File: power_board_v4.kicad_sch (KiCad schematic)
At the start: 21 parts, among them J1 Conn_01x02, J2 Conn_01x02, J3 Conn_01x02, J4 Conn_01x02, J5 Conn_01x02, J6 Conn_01x02, J7 Conn_01x02, Q1 PMOS, Q2 2SC1815, Q3 PMOS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

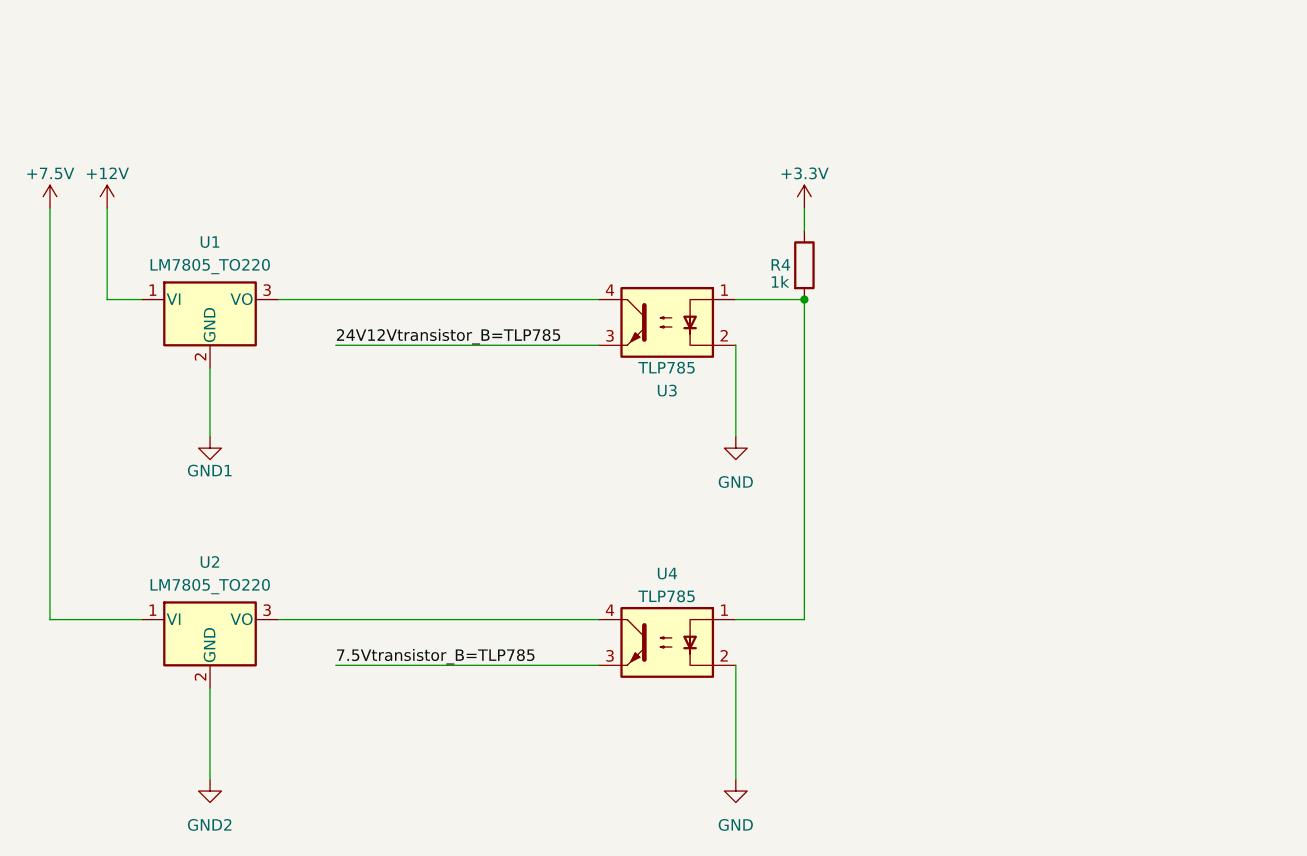
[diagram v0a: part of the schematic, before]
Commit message: レギュレーターとフォトカプラの周辺部品の追加
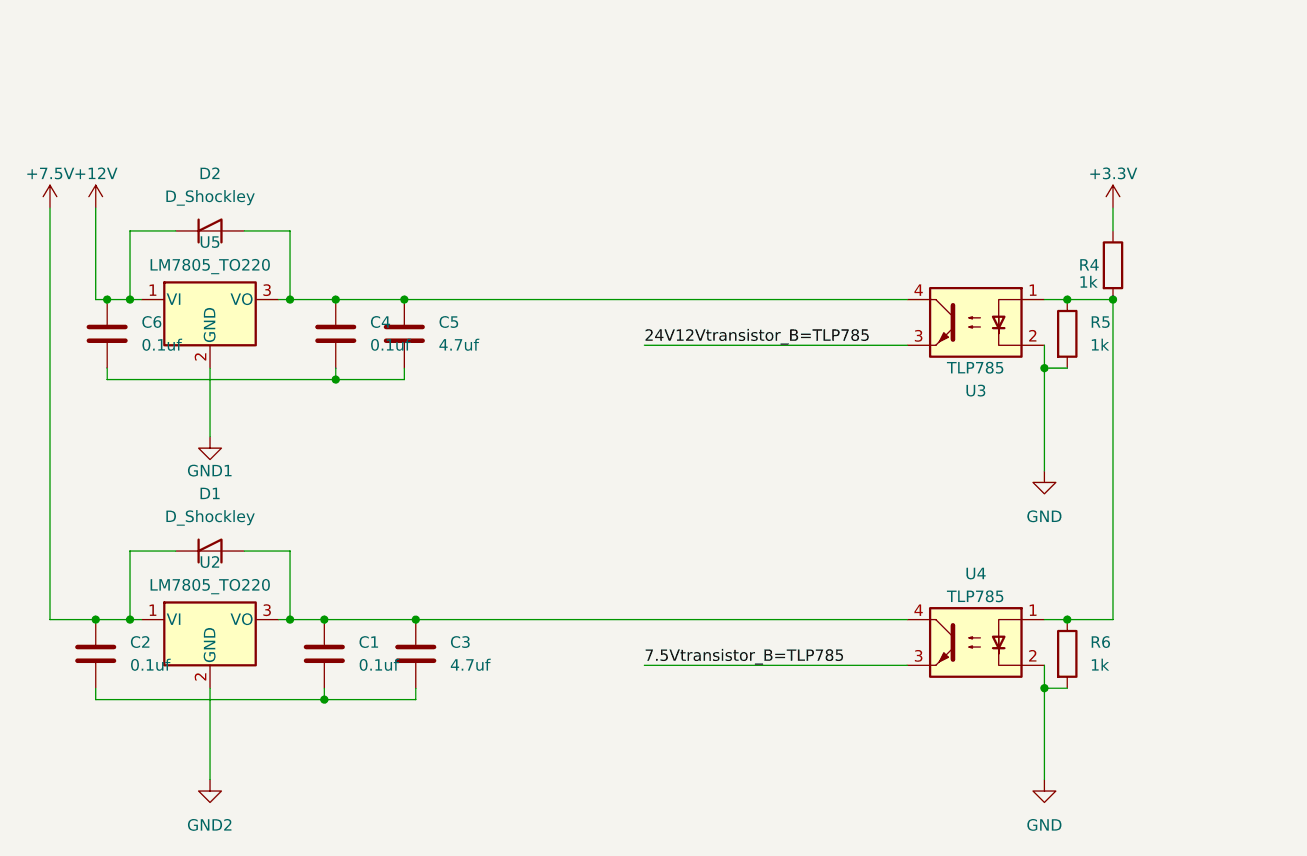
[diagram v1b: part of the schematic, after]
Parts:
- removed U1: LM7805_TO220, Package_TO_SOT_THT:TO-220-3_Vertical, symbol Regulator_Linear:LM7805_TO220
- added C1, C2, C4, C6: 0.1uf, symbol Device:C
- added C3, C5: 4.7uf, symbol Device:C
- added D1, D2: D_Shockley, symbol Device:D_Shockley
- added R5, R6: 1k, symbol Device:R
- added U5: LM7805_TO220, Package_TO_SOT_THT:TO-220-3_Vertical, symbol Regulator_Linear:LM7805_TO220
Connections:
- net +12V: now also C6.1, D2.1 (K), U5.1 (VI)
- net +7.5V: now also C2.1, D1.1 (K)
- net GND: now also R5.2, R6.2
- net GND1: now also U5.2 (GND)
- net at R4.2, U3.1, U4.1: now also R5.1, R6.1
- net at U3.4: now also C4.1, C5.1, D2.2 (A), U5.3 (VO)
- net at U2.3 (VO), U4.4: now also C1.1, C3.1, D1.2 (A)
- new net: C4.2, C5.2, C6.2
- new net: C1.2, C2.2, C3.2
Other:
- moved on the sheet: R4, U3, U4
